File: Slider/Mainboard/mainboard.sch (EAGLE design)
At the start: 60 parts, among them IC1 7805TV, IC2 33CV, IC3 LM358, Q1 16MHz, SW1 MS MOT1, SW2 MS MOT2, T1 BC337, T2 BC337, U1 ATMEGA328P_PDIP, U2 MAX232PTH

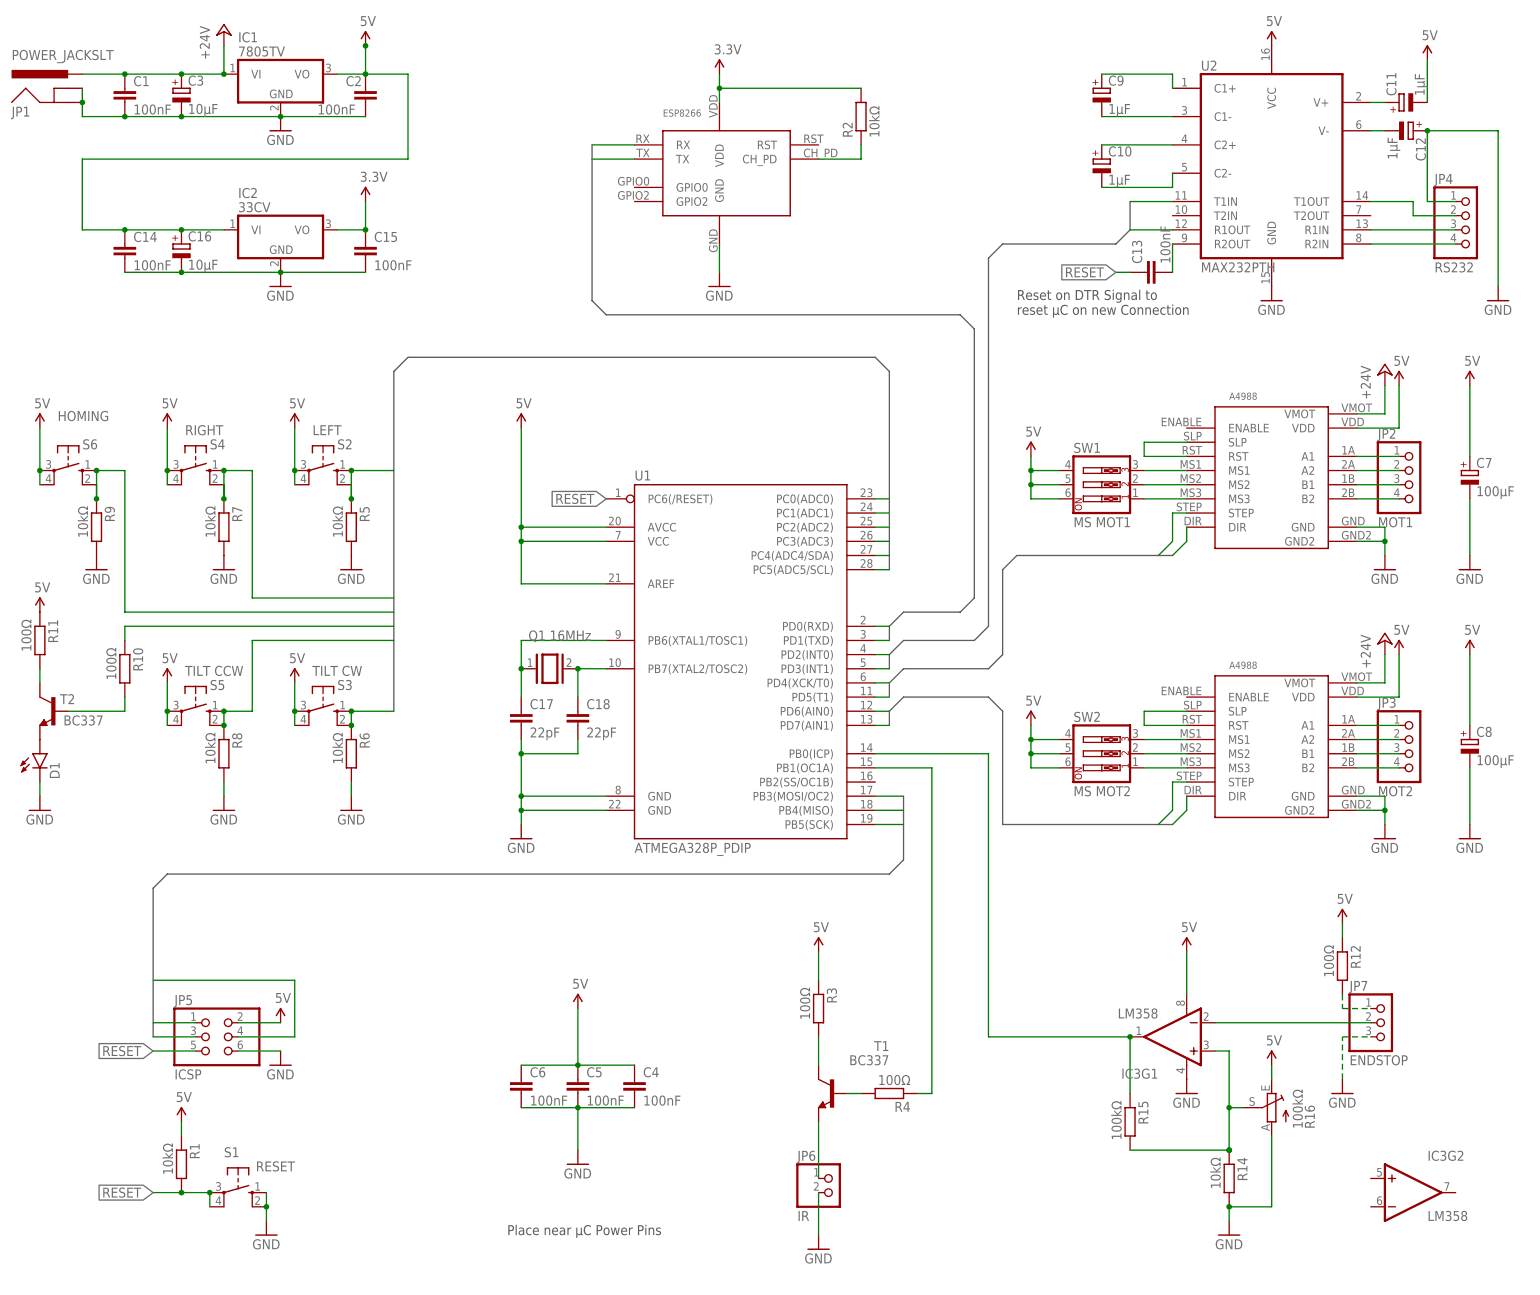
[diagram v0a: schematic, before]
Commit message: Started layouting seperate modules
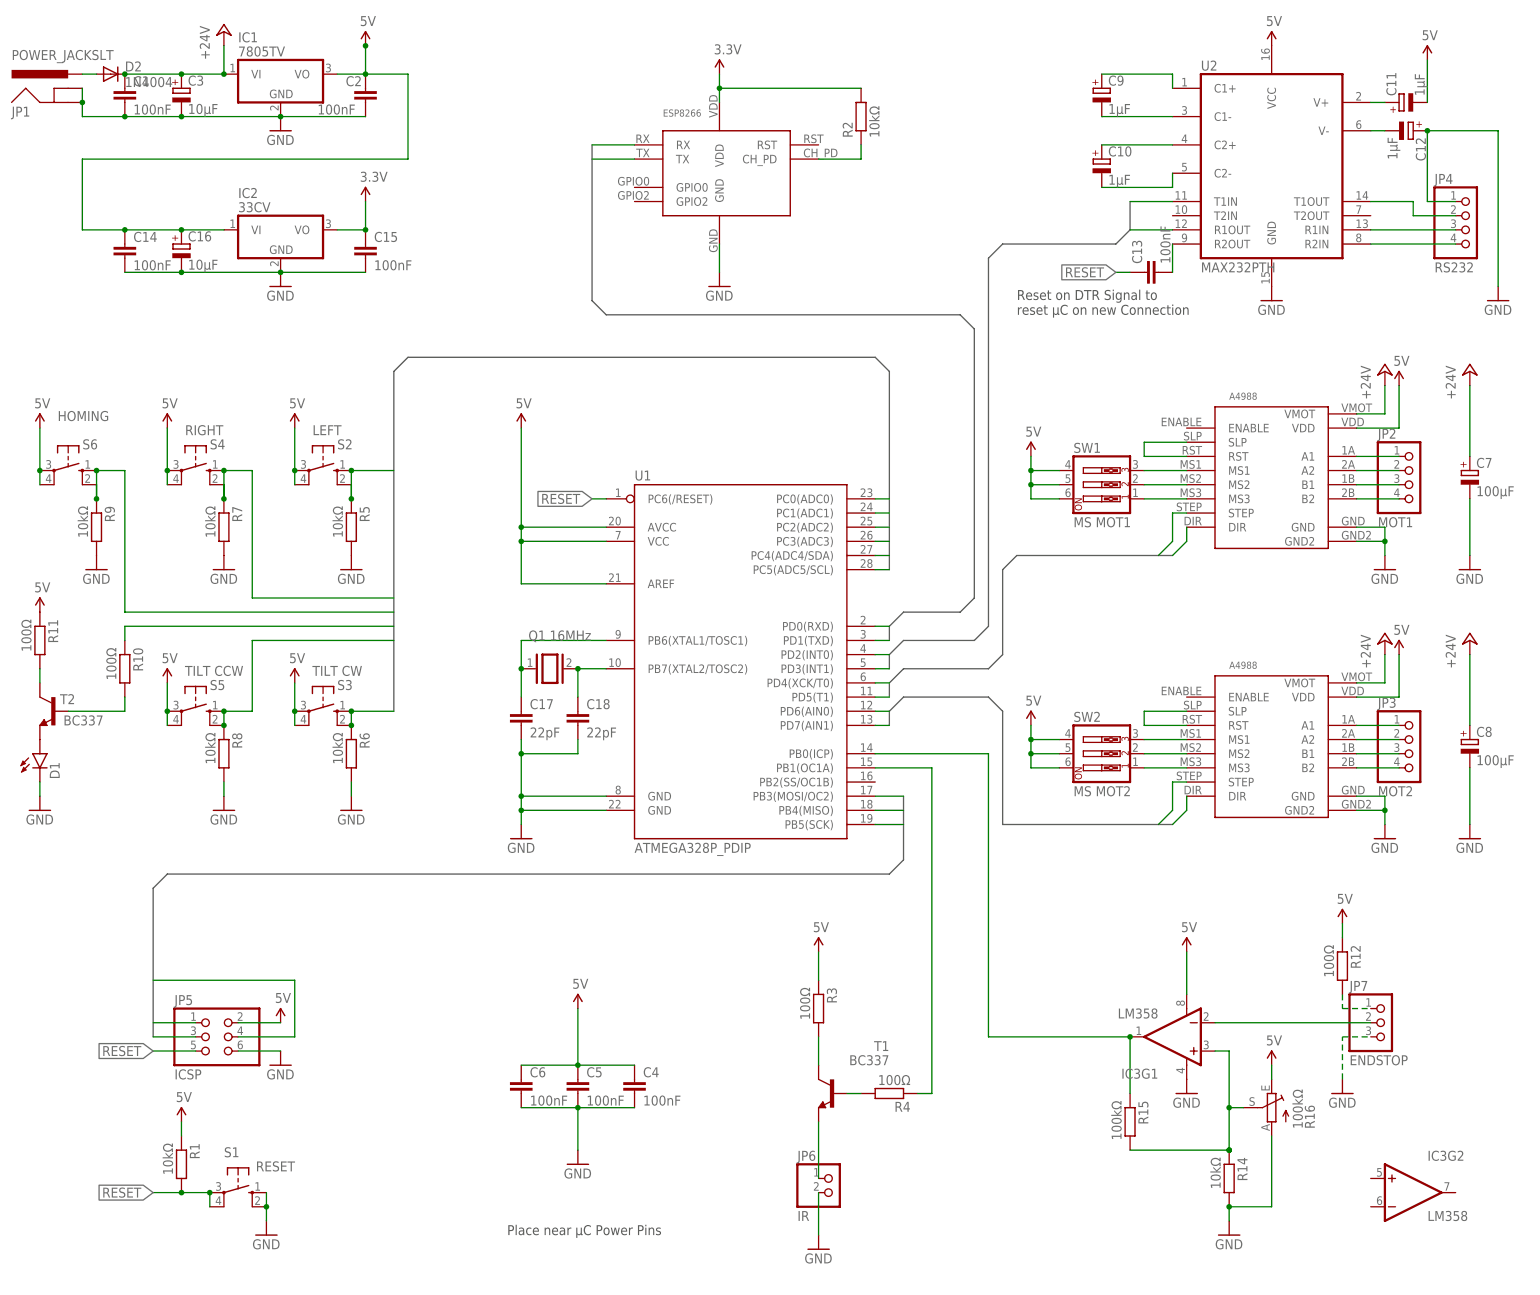
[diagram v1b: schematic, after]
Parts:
- added D2: 1N4004, diode:1N4004
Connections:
- new net N$41: D2.A, JP1.PWR
- net +24V: now also C7.+, C8.+, D2.C; no longer JP1.PWR
- net 5V: no longer C7.+, C8.+
- net RESET: now also U1.PC6(/RESET)
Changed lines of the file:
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@@
 <?xml version="1.0" encoding="utf-8"?>
 <!DOCTYPE eagle SYSTEM "eagle.dtd">
-<eagle version="7.3.0">
+<eagle version="6.5.0">
 <drawing>
 <settings>
@@
 <layers>
 <layer number="1" name="Top" color="4" fill="1" visible="no" active="no"/>
+<layer number="2" name="Route2" color="1" fill="3" visible="no" active="no"/>
+<layer number="3" name="Route3" color="4" fill="3" visible="no" active="no"/>
+<layer number="4" name="Route4" color="1" fill="4" visible="no" active="no"/>
+<layer number="5" name="Route5" color="4" fill="4" visible="no" active="no"/>
+<layer number="6" name="Route6" color="1" fill="8" visible="no" active="no"/>
+<layer number="7" name="Route7" color="4" fill="8" visible="no" active="no"/>
+<layer number="8" name="Route8" color="1" fill="2" visible="no" active="no"/>
+<layer number="9" name="Route9" color="4" fill="2" visible="no" active="no"/>
+<layer number="10" name="Route10" color="1" fill="7" visible="no" active="no"/>
+<layer number="11" name="Route11" color="4" fill="7" visible="no" active="no"/>
+<layer number="12" name="Route12" color="1" fill="5" visible="no" active="no"/>
+<layer number="13" name="Route13" color="4" fill="5" visible="no" active="no"/>
+<layer number="14" name="Route14" color="1" fill="6" visible="no" active="no"/>
+<layer number="15" name="Route15" color="4" fill="6" visible="no" active="no"/>
 <layer number="16" name="Bottom" color="1" fill="1" visible="no" active="no"/>
 <layer number="17" name="Pads" color="2" fill="1" visible="no" active="no"/>
@@
 <part name="JP2" library="pinhead" deviceset="PINHD-1X4" device="" value="MOT1"/>
 <part name="C7" library="rcl" deviceset="CPOL-EU" device="E2,5-6E" value="100µF"/>
-<part name="SUPPLY4" library="SparkFun-Aesthetics" deviceset="5V" device=""/>
 <part name="GND6" library="supply1" deviceset="GND" device=""/>
 <part name="U$2" library="parts" deviceset="A4988" device=""/>
@@
 <part name="JP3" library="pinhead" deviceset="PINHD-1X4" device="" value="MOT2"/>
 <part name="C8" library="rcl" deviceset="CPOL-EU" device="E2,5-6E" value="100µF"/>
-<part name="SUPPLY9" library="SparkFun-Aesthetics" deviceset="5V" device=""/>
 <part name="GND8" library="supply1" deviceset="GND" device=""/>
 <part name="U2" library="SparkFun-DigitalIC" deviceset="MAX232" device="PTH"/>
@@
 <part name="SUPPLY25" library="SparkFun-Aesthetics" deviceset="5V" device=""/>
 <part name="R16" library="pot" deviceset="TRIM_EU-" device="CA9V" value="100kΩ"/>
+<part name="D2" library="diode" deviceset="1N4004" device=""/>
+<part name="P+4" library="supply1" deviceset="+24V" device=""/>
+<part name="P+5" library="supply1" deviceset="+24V" device=""/>
 </parts>
 <sheets>
@@
 <instance part="JP2" gate="A" x="137.16" y="83.82"/>
 <instance part="C7" gate="G$1" x="147.32" y="86.36"/>
-<instance part="SUPPLY4" gate="G$1" x="147.32" y="101.6"/>
 <instance part="GND6" gate="1" x="147.32" y="68.58"/>
 <instance part="U$2" gate="G$1" x="114.3" y="35.56"/>
@@
 <instance part="JP3" gate="A" x="137.16" y="35.56"/>
 <instance part="C8" gate="G$1" x="147.32" y="38.1"/>
-<instance part="SUPPLY9" gate="G$1" x="147.32" y="53.34"/>
 <instance part="GND8" gate="1" x="147.32" y="20.32"/>
 <instance part="U2" gate="G$1" x="109.22" y="142.24"/>
@@
 <instance part="SUPPLY25" gate="G$1" x="-83.82" y="-30.48"/>
 <instance part="R16" gate="1" x="111.76" y="-27.94" rot="MR0"/>
+<instance part="D2" gate="1" x="-96.52" y="157.48"/>
+<instance part="P+4" gate="1" x="147.32" y="55.88"/>
+<instance part="P+5" gate="1" x="147.32" y="104.14"/>
 </instances>
 <busses>
@@
 <net name="+24V" class="0">
 <segment>
-<pinref part="JP1" gate="G$1" pin="PWR"/>
 <pinref part="IC1" gate="A1" pin="VI"/>
 <wire x1="-76.2" y1="157.48" x2="-83.82" y2="157.48" width="0.1524" layer="91"/>
@@
 <junction x="-76.2" y="157.48"/>
 <wire x1="-83.82" y1="157.48" x2="-93.98" y2="157.48" width="0.1524" layer="91"/>
-<wire x1="-93.98" y1="157.48" x2="-101.6" y2="157.48" width="0.1524" layer="91"/>
 <wire x1="-76.2" y1="157.48" x2="-76.2" y2="162.56" width="0.1524" layer="91"/>
 <pinref part="C1" gate="G$1" pin="1"/>
-<junction x="-93.98" y="157.48"/>
 <pinref part="C3" gate="G$1" pin="+"/>
 <junction x="-83.82" y="157.48"/>
+<pinref part="D2" gate="1" pin="C"/>
+<junction x="-93.98" y="157.48"/>
 </segment>
 <segment>
@@
 <pinref part="P+3" gate="1" pin="+24V"/>
 <wire x1="132.08" y1="48.26" x2="132.08" y2="53.34" width="0.1524" layer="91"/>
+</segment>
+<segment>
+<pinref part="C8" gate="G$1" pin="+"/>
+<wire x1="147.32" y1="53.34" x2="147.32" y2="40.64" width="0.1524" layer="91"/>
+<pinref part="P+4" gate="1" pin="+24V"/>
+</segment>
+<segment>
+<pinref part="C7" gate="G$1" pin="+"/>
+<wire x1="147.32" y1="101.6" x2="147.32" y2="88.9" width="0.1524" layer="91"/>
+<pinref part="P+5" gate="1" pin="+24V"/>
 </segment>
 </net>
@@
 </segment>
 <segment>
-<pinref part="C7" gate="G$1" pin="+"/>
-<pinref part="SUPPLY4" gate="G$1" pin="5V"/>
-<wire x1="147.32" y1="101.6" x2="147.32" y2="88.9" width="0.1524" layer="91"/>
-</segment>
-<segment>
 <pinref part="SUPPLY7" gate="G$1" pin="5V"/>
 <wire x1="68.58" y1="40.64" x2="68.58" y2="38.1" width="0.1524" layer="91"/>
@@
 </segment>
 <segment>
-<pinref part="C8" gate="G$1" pin="+"/>
-<pinref part="SUPPLY9" gate="G$1" pin="5V"/>
-<wire x1="147.32" y1="53.34" x2="147.32" y2="40.64" width="0.1524" layer="91"/>
-</segment>
-<segment>
 <pinref part="U2" gate="G$1" pin="VCC"/>
 <pinref part="SUPPLY10" gate="G$1" pin="5V"/>
@@
 <wire x1="-83.82" y1="-43.18" x2="-78.74" y2="-43.18" width="0.1524" layer="91"/>
 <wire x1="-78.74" y1="-43.18" x2="-78.74" y2="-45.72" width="0.1524" layer="91"/>
-<label x="-7.62" y="81.28" size="1.778" layer="95" rot="R180" xref="yes"/>
+<label x="-10.16" y="81.28" size="1.778" layer="95" rot="R180" xref="yes"/>
 <pinref part="S1" gate="1" pin="P"/>
 <junction x="-78.74" y="-43.18"/>
@@
 <wire x1="-81.28" y1="-17.78" x2="-88.9" y2="-17.78" width="0.1524" layer="91"/>
 <label x="-88.9" y="-17.78" size="1.778" layer="95" rot="MR0" xref="yes"/>
+</segment>
+<segment>
+<pinref part="U1" gate="G$1" pin="PC6(/RESET)"/>
+<wire x1="-7.62" y1="81.28" x2="-10.16" y2="81.28" width="0.1524" layer="91"/>
 </segment>
 </net>
@@
 </segment>
 </net>
+<net name="N$41" class="0">
+<segment>
+<pinref part="D2" gate="1" pin="A"/>
+<pinref part="JP1" gate="G$1" pin="PWR"/>
+<wire x1="-99.06" y1="157.48" x2="-101.6" y2="157.48" width="0.1524" layer="91"/>
+</segment>
+</net>

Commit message: Further board layouting
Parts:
- R1, R10, R11, R12, R14, R15, R2, R3, R4, R5, R6, R7, R8, R9: device rcl:R-EU_0411/15 -> rcl:R-EU_0207/7
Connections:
- removed net DIR: U$1.DIR, U$2.DIR, U1.PD5(T1), U1.PD7(AIN1)
- removed net MOSI: JP5.4, U1.PB3(MOSI/OC2)
- removed net STEP: U$1.STEP, U$2.STEP, U1.PD4(XCK/T0), U1.PD6(AIN0)
- new net DIR1: U$1.DIR, U1.PC1(ADC1)
- new net DIR2: U$2.DIR, U1.PC3(ADC3)
- new net STEP1: U$1.STEP, U1.PC2(ADC2)
- new net STEP2: U$2.STEP, U1.PC4(ADC4/SDA)
- net HOMING: now also JP5.4, U1.PB3(MOSI/OC2); no longer U1.PC4(ADC4/SDA)
- net LEFT: now also U1.PD5(T1); no longer U1.PC0(ADC0)
- net N$31: now also U1.PB0(ICP); no longer U1.PB1(OC1A)
- net N$38: now also U1.PC5(ADC5/SCL); no longer U1.PB0(ICP)
- net RIGHT: now also U1.PD7(AIN1); no longer U1.PC1(ADC1)
- net RXD: now also U1.PD3(INT1); no longer U1.PD2(INT0)
- net STATUS: now also U1.PB2(SS/OC1B); no longer U1.PC5(ADC5/SCL)
- net TILTCCW: now also U1.PD6(AIN0); no longer U1.PC3(ADC3)
- net TILTCW: now also U1.PB1(OC1A); no longer U1.PC2(ADC2)
- net TXD: now also U1.PD2(INT0); no longer U1.PD3(INT1)
